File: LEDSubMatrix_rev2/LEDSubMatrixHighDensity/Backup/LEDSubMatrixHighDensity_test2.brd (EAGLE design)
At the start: 16.9 x 146 mm, 138 parts, among them IC1 TLC5955DCAR, IC2 TLC5955DCAR, IC3 TLC5955DCAR, IC4 TLC5955DCAR, IC5 TLC5955DCAR, IC6 TLC5955DCAR, IC7 TLC5955DCAR, IC8 TLC5955DCAR

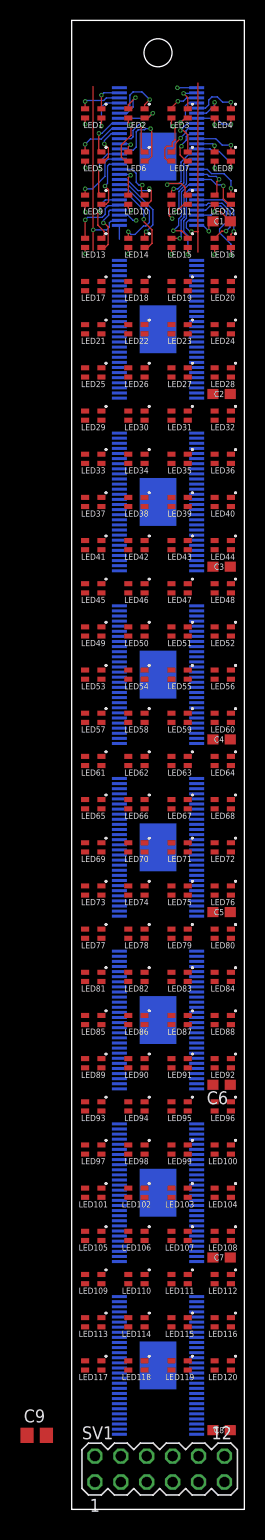
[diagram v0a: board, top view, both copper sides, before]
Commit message: Updated pinouts to align with control board
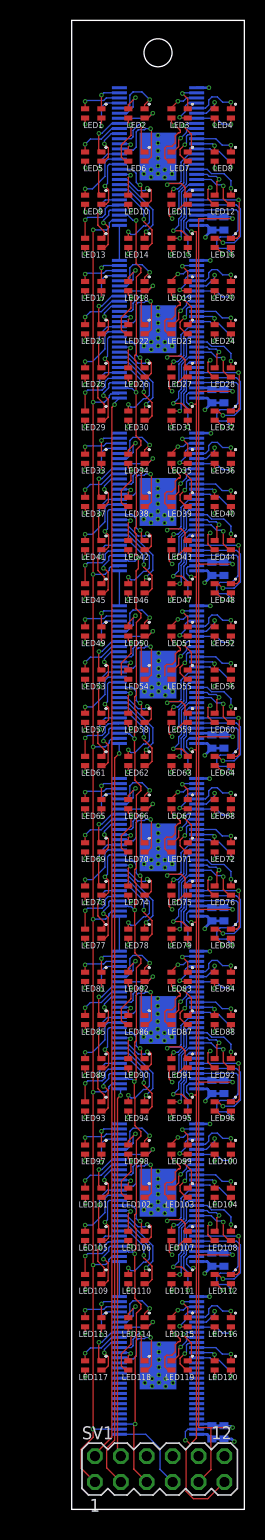
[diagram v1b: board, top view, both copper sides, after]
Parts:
- removed C9: 20uF, rcl:C0805
- added C1B, C2B, C3B, C4B, C5B, C6B, C7B, C8B: 10uF, rcl:C0402
- C1, C2, C3, C4, C5, C6, C7, C8: value 20uF -> .1uF; device rcl:C0603 -> rcl:C0402
- moved C6 0.97 mm to (13.8, -104.6), flipped to the bottom, turned to 270 degrees
- moved C7 0.97 mm to (13.8, -121.5), flipped to the bottom, turned to 270 degrees
- moved C8 0.97 mm to (13.8, -138.4), flipped to the bottom, turned to 270 degrees
- moved C1 0.97 mm to (13.8, -19.9), flipped to the bottom, turned to 270 degrees
- moved C2 0.97 mm to (13.8, -36.8), flipped to the bottom, turned to 270 degrees
- moved C3 0.97 mm to (13.8, -53.8), flipped to the bottom, turned to 270 degrees
- moved C4 0.97 mm to (13.8, -70.7), flipped to the bottom, turned to 270 degrees
- moved C5 0.97 mm to (13.8, -87.6), flipped to the bottom, turned to 270 degrees
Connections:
- new net 3V3_LOGIC: C1.1, C1B.1, C2.1, C2B.1, C3.1, C3B.1, C4.1, C4B.1, C5.1, C5B.1, C6.1, C6B.1, C7.1, C7B.1, C8.1, C8B.1, IC1.54, IC2.54, IC3.54, IC4.54, IC5.54, IC6.54, IC7.54, IC8.54, SV1.9
- net 3V3: no longer C1.1, C2.1, C3.1, C4.1, C5.1, C6.1, C7.1, C8.1, C9.1, IC1.54, IC2.54, IC3.54, IC4.54, IC5.54, IC6.54, IC7.54, IC8.54
- net GND: now also C1B.2, C2B.2, C3B.2, C4B.2, C5B.2, C6B.2, C7B.2, C8B.2; no longer C9.2, SV1.9
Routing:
- net 3V3_LOGIC: track 0.00 -> 180.4 mm, vias 0 -> 8
- net 3V3: track 23.5 -> 165.8 mm, vias 14 -> 104
- net LAT: track 1.85 -> 142.2 mm, vias 1 -> 8
- net GSCLK: track 19.5 -> 150.7 mm, vias 1 -> 8
- net SCLK: track 19.3 -> 147.8 mm, vias 1 -> 8
- net SIN_1,2: track 0.00 -> 104.7 mm, vias 0 -> 1
- net SIN_3,4: track 0.00 -> 73.5 mm, vias 0 -> 1
- net GND: track 4.46 -> 41.6 mm, vias 2 -> 112
- net SIN_5,6: track 0.00 -> 36.3 mm, vias 0 -> 1
- net N$LEDB96: track 0.00 -> 11.6 mm, vias 0 -> 1
- net N$LEDB48: track 0.00 -> 11.6 mm, vias 0 -> 1
- net N$LEDB32: track 0.00 -> 11.6 mm, vias 0 -> 1
- net N$LEDB80: track 0.00 -> 11.6 mm, vias 0 -> 1
- net N$LEDB64: track 0.00 -> 11.6 mm, vias 0 -> 1
- net N$LEDB112: track 0.00 -> 11.6 mm, vias 0 -> 1
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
